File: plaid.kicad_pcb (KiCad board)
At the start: 2 copper layers, 228 x 98 mm, 140 parts, among them J2 AVR_ISP_6, J3 Conn_01x04, J4 GS2, J5 GS2, SW1 SW_Push, SW10 SW_Push, SW11 SW_Push, SW12 SW_Push, SW13 SW_Push, SW14 SW_Push, SW15 SW_Push, SW16 SW_Push, SW17 SW_Push, SW18 SW_Push, SW19 SW_Push, SW2 SW_Push, SW20 SW_Push, SW21 SW_Push, SW22 SW_Push, SW23 SW_Push, SW24 SW_Push, SW25 SW_Push, SW26 SW_Push, SW27 SW_Push, SW28 SW_Push, SW29 SW_Push, SW3 SW_Push, SW30 SW_Push, SW31 SW_Push, SW32 SW_Push, SW33 SW_Push, SW34 SW_Push, SW35 SW_Push, SW36 SW_Push, SW37 SW_Push, SW38 SW_Push, SW39 SW_Push, SW4 SW_Push, SW40 SW_Push, SW41 SW_Push, SW42 SW_Push, SW43 SW_Push, SW44 SW_Push, SW45 SW_Push, SW46 SW_Push, SW47 SW_Push, SW48 SW_Push, SW49 SW_Push, SW5 SW_Push, SW50 RESET, SW51 BOOT, SW6 SW_Push, SW7 SW_Push, SW8 SW_Push, SW9 SW_Push, U1 ATMEGA328-PU, Y1 16MHz

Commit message: fixing spacebar footprints
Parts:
- SW49: footprint SMKJP:SW_Cherry_MX1A_1.00u_PCB -> MX_Alps_Hybrid:MXOnly-2U-ReversedStabilizers-NoLED
- turned SW43 to 0 degrees
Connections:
- SW43 pad 1: /COL6 -> Net-(D42-Pad2)
- SW43 pad 2: Net-(D42-Pad2) -> /COL6
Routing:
- net /COL6: track 125.8 -> 116.7 mm
- net Net-(D42-Pad2): track 114.0 -> 105.8 mm

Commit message: adding 2x2u layout
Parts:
- added SW49: SW_Push, MX_Alps_Hybrid:MXOnly-2U-ReversedStabilizers-NoLED, F.Cu at (183.1, 138.5)
- added SW49: SW_Push, MX_Alps_Hybrid:MXOnly-2U-ReversedStabilizers-NoLED, F.Cu at (144.9, 138.5)
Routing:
- net Net-(D42-Pad2): track 105.8 -> 115.4 mm
- net /COL4: track 168.5 -> 178.0 mm
- net Net-(D41-Pad2): track 87.8 -> 97.3 mm
- net /COL6: track 116.7 -> 124.4 mm
- net /COL7: track 98.8 -> 102.0 mm
- net /COL5: track 158.5 -> 161.6 mm
- net GND: vias 79 -> 82
- added copper zone on B.Cu, net /COL4
- added copper zone on B.Cu, net /COL6
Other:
- board text added: "Plaid // Through Hole // Rev.Cx2u (c)2018 Takuya Urakawa, Dm9Records.com USBC and 2u layout added by Worldspawn00"
- board text removed: "Plaid // Through Hole // Rev.Alpha (c)2018 Takuya Urakawa, Dm9Records.com"

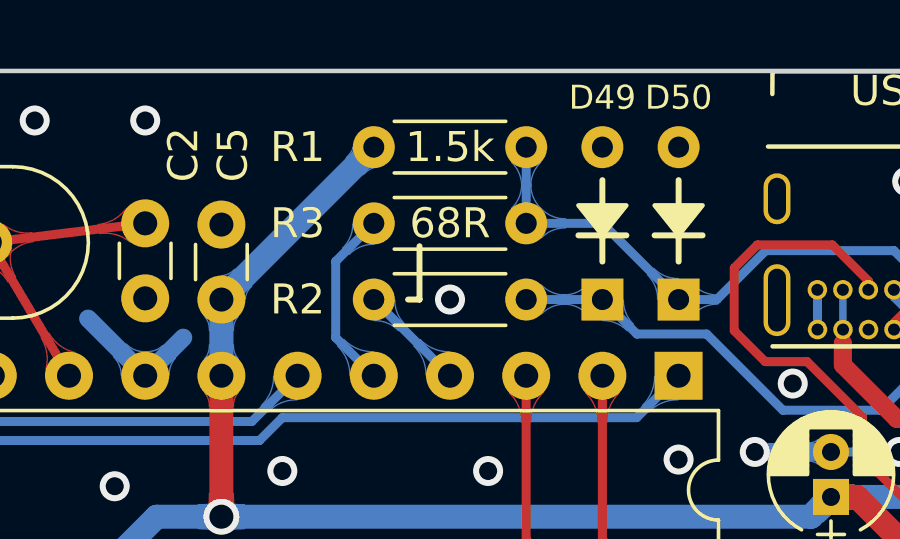
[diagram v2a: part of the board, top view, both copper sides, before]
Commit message: fix resistor value
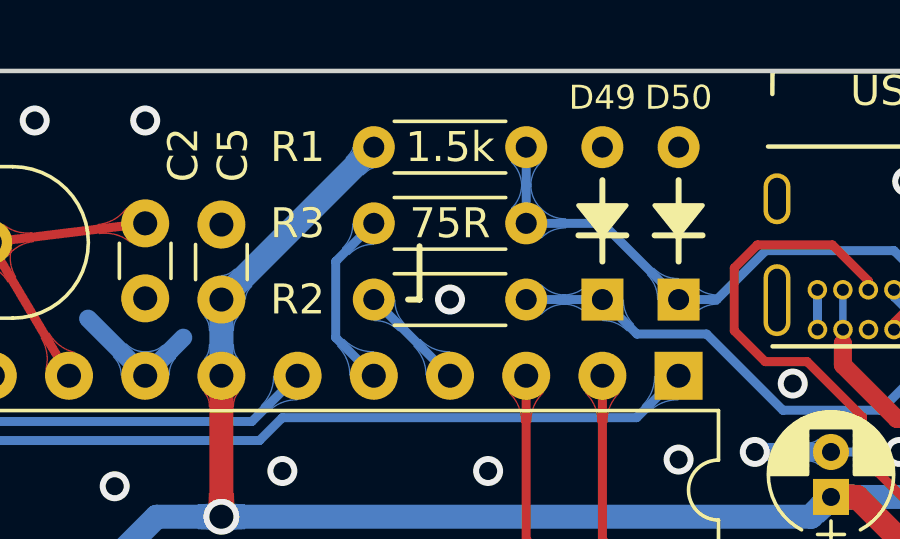
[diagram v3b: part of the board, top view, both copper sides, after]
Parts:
- R3: value 68R -> 75R
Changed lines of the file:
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@@
       (effects (font (size 1 1) (thickness 0.15)))
     )
-    (fp_text value 68R (at 2.54 0) (layer F.SilkS)
+    (fp_text value 75R (at 2.54 0) (layer F.SilkS)
       (effects (font (size 1 1) (thickness 0.15)))
     )
